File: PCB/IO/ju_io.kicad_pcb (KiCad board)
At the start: 2 copper layers, 30 x 65 mm, 17 parts, among them J1 Conn_01x05, J2 Conn_01x05, J3 Conn_01x05, J4 Conn_01x05, J5 Conn_01x03, J6 Conn_01x03, U1 PiPico_No_SWD

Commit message: PCBs of v1.1
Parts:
- removed J6: Conn_01x03, ju_io:SH1.0_3P
- added D1: WS2812B_Unified, ju_io:WS2812B-2835, F.Cu at (138.6, 121.7)
- added D2: WS2812B_Unified, ju_io:WS2812B-2835, F.Cu at (138.6, 110.7)
- added D3: WS2812B_Unified, ju_io:WS2812B-2835, F.Cu at (138.6, 99.7)
- added D4: WS2812B_Unified, ju_io:WS2812B-2835, F.Cu at (138.6, 88.7)
- U1: footprint ju_io:RPi_Pico_SMD_Pins_No_SWD -> ju_io:RPi_Pico_SMD_Pins_No_SWD_No_Text
- moved R3 34.0 mm to (130.5, 128.6), turned to 0 degrees
- moved R4 28.8 mm to (143.2, 76.8), turned to 0 degrees
- moved J5 25.1 mm to (146.1, 70.7), turned to 180 degrees
- moved J1 12.4 mm to (145.1, 85.7)
- moved J2 12.4 mm to (145.1, 96.7)
- moved R2 5.91 mm to (128.9, 77.8), turned to 180 degrees
- moved R1 5.75 mm to (128.9, 76.2), turned to 180 degrees
- moved C1 4.76 mm to (141.7, 105.4), turned to 0 degrees
- moved J3 4.24 mm to (145.1, 112.7)
- moved J4 4.24 mm to (145.1, 123.7)
- moved B1 3.50 mm to (130.6, 88.7)
- moved B2 3.50 mm to (130.6, 99.7)
- moved B3 3.50 mm to (130.6, 110.7)
- moved B4 3.50 mm to (130.6, 121.7)
- moved U1 3.00 mm to (137.1, 105.7)
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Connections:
- R3 pad 2: Net-(J5-Pin_2) -> Net-(D1-In)
- R4 pad 1: Net-(U1-GPIO16) -> Net-(U1-GPIO28_ADC2)
- R4 pad 2: Net-(J6-Pin_2) -> Net-(J5-Pin_2)
- U1 pad 21: Net-(U1-GPIO16) -> unconnected-(U1-GPIO16-Pad21)
- U1 pad 34: unconnected-(U1-GPIO28_ADC2-Pad34) -> Net-(U1-GPIO28_ADC2)
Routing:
- net Net-(U1-GPIO17): track 40.0 -> 2.83 mm
- net Net-(U1-GPIO16): track 32.4 -> 0.00 mm, vias 1 -> 0
- net Net-(U1-GPIO28_ADC2): track 0.00 -> 28.0 mm, vias 0 -> 1
- net +5V: track 40.5 -> 68.4 mm, vias 2 -> 1
- net Net-(J2-Pin_1): track 29.0 -> 8.01 mm
- net Net-(J2-Pin_3): track 20.5 -> 3.85 mm
- net GND: track 33.0 -> 16.4 mm, vias 15 -> 17
- net Net-(J1-Pin_1): track 27.5 -> 12.0 mm
- net Net-(J2-Pin_2): track 26.1 -> 11.1 mm
- net Net-(J1-Pin_2): track 24.3 -> 10.2 mm
- net Net-(J1-Pin_3): track 18.5 -> 4.46 mm
- net Net-(D1-In): track 0.00 -> 11.2 mm
- net Net-(B4-A): track 0.00 -> 10.3 mm
- net Net-(J2-Pin_4): track 18.5 -> 9.79 mm
- net Net-(D3-Out): track 0.00 -> 8.55 mm
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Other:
- board size 30 x 65 mm -> 26 x 65 mm
- board text added: "IO v1.1"
- board text removed: "IO v1.0"
- board text removed: "JLCJLCJLCJLC"

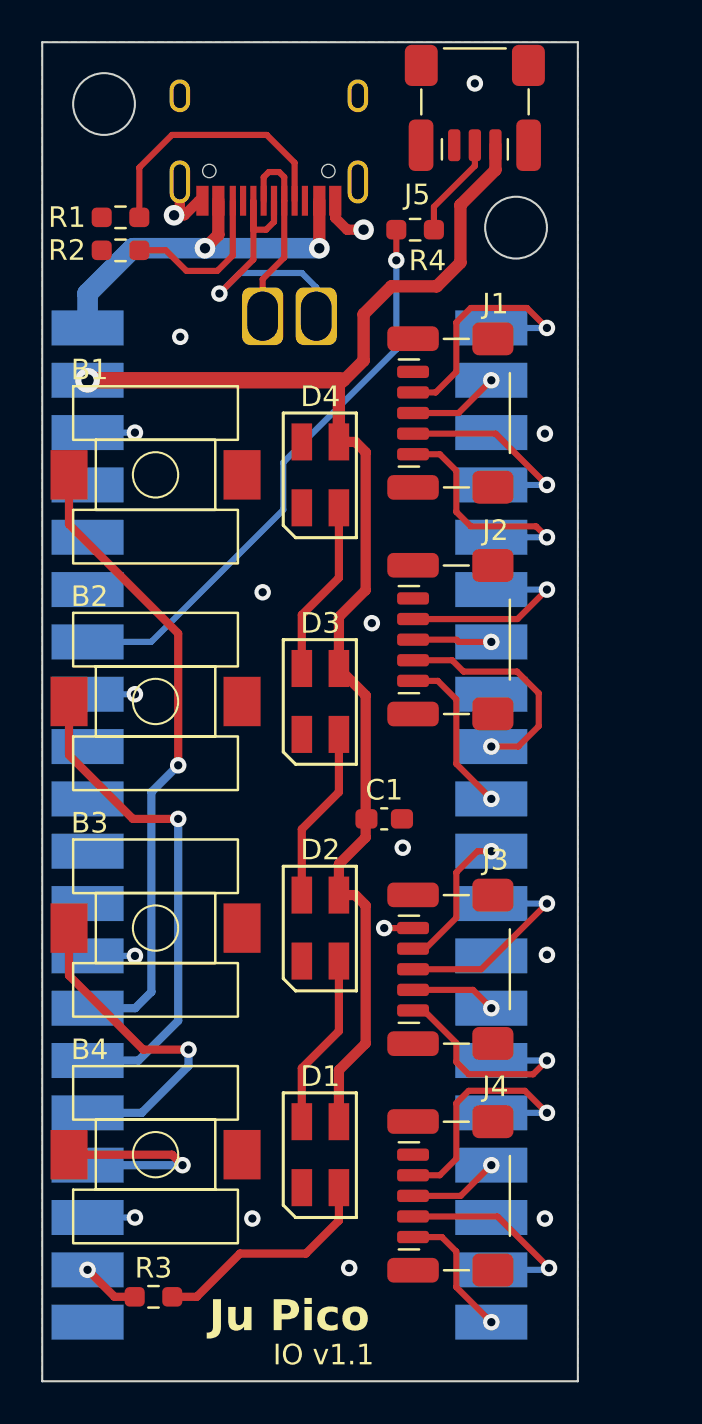
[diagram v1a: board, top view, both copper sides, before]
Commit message: PCB optimization button v1.2, io v1.21
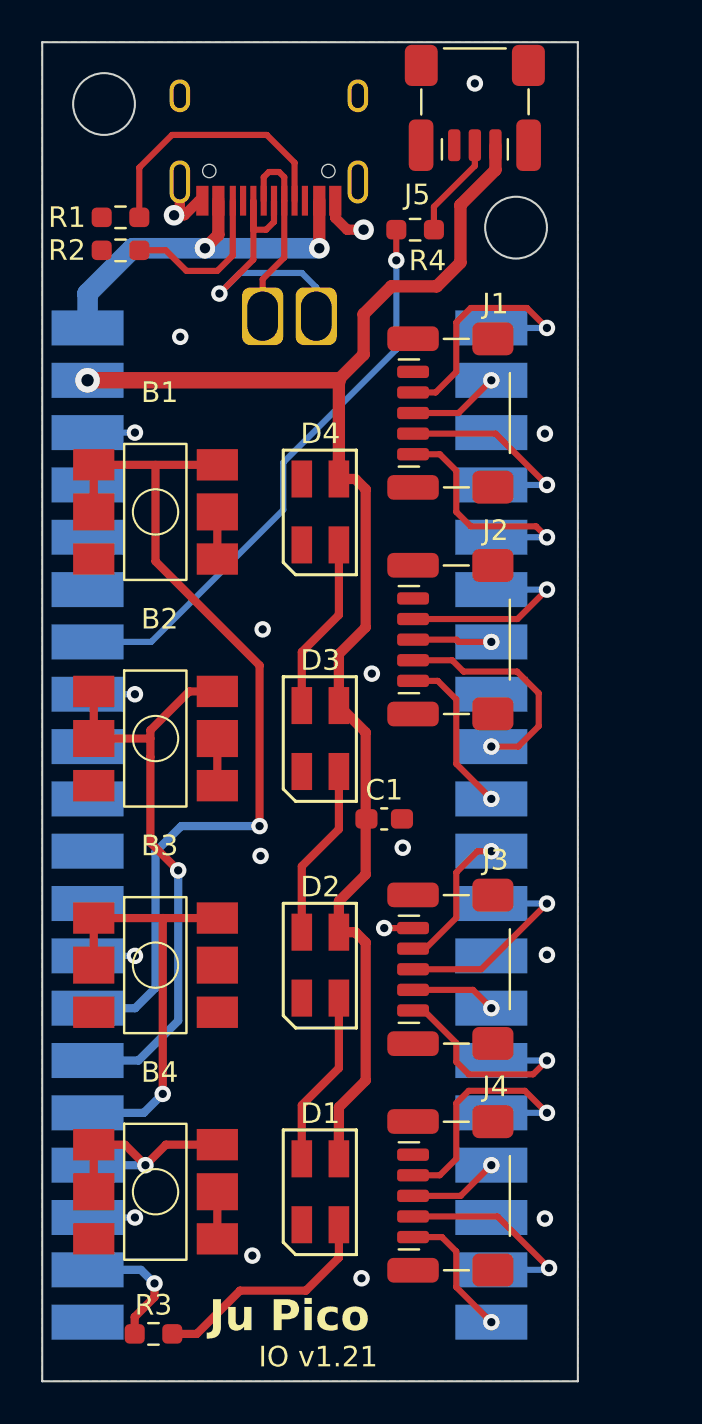
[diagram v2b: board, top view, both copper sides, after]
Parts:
- B1, B2, B3, B4: footprint ju_io:SKSTAAE010 -> ju_io:EVQP1K05M
- moved B1 1.80 mm to (130.6, 90.5)
- moved B2 1.80 mm to (130.6, 101.5)
- moved B3 1.80 mm to (130.6, 112.5)
- moved B4 1.80 mm to (130.6, 123.5)
- moved D1 1.80 mm to (138.6, 123.5)
- moved D2 1.80 mm to (138.6, 112.5)
- moved D3 1.80 mm to (138.6, 101.5)
- moved D4 1.80 mm to (138.6, 90.5)
- moved R3 1.80 mm to (130.5, 130.4)
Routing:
- net Net-(B1-A): track 31.3 -> 43.8 mm
- net GND: track 16.4 -> 23.3 mm, vias 17 -> 18
- net Net-(B2-A): track 24.2 -> 28.9 mm
- net Net-(B3-A): track 16.2 -> 20.9 mm
- net Net-(U1-GPIO17): track 2.83 -> 6.37 mm
- net +5V: track 68.4 -> 70.0 mm
- net Net-(B4-A): track 10.3 -> 11.9 mm
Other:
- board text added: "IO v1.21"
- board text removed: "IO v1.1"

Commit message: Ju Pico IO PCB v1.22
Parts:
- removed R3, R4: 10, Resistor_SMD:R_0603_1608Metric_Pad0.98x0.95mm_HandSolder
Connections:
- U1 pad 22: Net-(U1-GPIO17) -> Net-(D1-In)
- U1 pad 34: Net-(U1-GPIO28_ADC2) -> Net-(J5-Pin_2)
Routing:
- net Net-(J5-Pin_2): track 4.92 -> 33.7 mm, vias 0 -> 1
- net Net-(U1-GPIO28_ADC2): track 28.0 -> 0.00 mm, vias 1 -> 0
- net Net-(U1-GPIO17): track 6.37 -> 0.00 mm, vias 1 -> 0
- net Net-(D1-In): track 11.2 -> 14.6 mm, vias 0 -> 1
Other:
- board text added: "IO v1.22"
- board text removed: "IO v1.21"

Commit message: Ju IO PCB v1.3 (just text change)
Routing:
- net +5V: track 70.0 -> 69.4 mm
- net Net-(J5-Pin_2): track 33.7 -> 34.2 mm
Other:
- board text added: "Ju Pico IO v1.3"
- board text added: "github.com/whowechina"
- board text removed: "IO v1.22"
- board text removed: "Ju Pico"
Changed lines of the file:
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@@
 			(psa4output no)
 			(plot_black_and_white yes)
-			(plotinvisibletext no)
 			(sketchpadsonfab no)
 			(plotpadnumbers no)
@@
 			(at 0 3.98 0)
 			(layer "F.Fab")
+			(hide yes)
 			(effects
 				(font
@@
 			(layer "B.Fab")
 		)
-		(fp_text user "Copper Keepouts shown on Dwgs layer"
-			(at 0.1 30.2 0)
-			(layer "Cmts.User")
-			(hide yes)
-			(effects
-				(font
-					(size 1 1)
-					(thickness 0.15)
-				)
-			)
-		)
 		(fp_text user "${REFERENCE}"
 			(at 0 0 0)
@@
 		(layer "Edge.Cuts")
 	)
-	(gr_text "IO v1.22"
-		(at 135.32 132.08 0)
+	(gr_text "github.com/whowechina"
+		(at 128.35 131.66 0)
 		(layer "F.SilkS")
 		(effects
@@
 		)
 	)
-	(gr_text "Ju Pico"
-		(at 133.17 130.38 0)
+	(gr_text "Ju Pico IO v1.3"
+		(at 129.95 130.18 0)
 		(layer "F.SilkS")
 		(effects
 			(font
-				(size 1.5 1.5)
-				(thickness 0.3)
+				(size 1.25 1.25)
+				(thickness 0.24)
 				(bold yes)
 			)
@@
 	)
 	(segment
+		(start 145.37 75.85)
+		(end 147.07 74.15)
+		(width 0.6)
+		(layer "F.Cu")
+		(net 2)
+	)
+	(segment
 		(start 139.47 99.88)
 		(end 140.77 101.18)
@@
 	)
 	(segment
-		(start 145.37 75.58)
-		(end 147.07 73.88)
+		(start 140.67 82.84)
+		(end 140.67 80.88)
 		(width 0.6)
 		(layer "F.Cu")
@@
 	)
 	(segment
-		(start 139.47 84.14)
-		(end 139.47 88.88)
+		(start 140.67 80.88)
+		(end 142.02 79.53)
 		(width 0.6)
 		(layer "F.Cu")
@@
 	)
 	(segment
-		(start 140.27 110.88)
-		(end 140.77 111.38)
-		(width 0.5)
+		(start 143.14 79.53)
+		(end 145.37 77.3)
+		(width 0.6)
 		(layer "F.Cu")
 		(net 2)
 	)
 	(segment
-		(start 139.42 84.09)
-		(end 140.67 82.84)
+		(start 147.07 74.15)
+		(end 147.07 72.68)
 		(width 0.6)
 		(layer "F.Cu")
@@
 	)
 	(segment
-		(start 140.67 80.88)
-		(end 142.02 79.53)
+		(start 139.47 84.14)
+		(end 139.47 88.88)
 		(width 0.6)
 		(layer "F.Cu")
@@
 	)
 	(segment
-		(start 140.77 108.08)
-		(end 139.47 109.38)
+		(start 140.27 110.88)
+		(end 140.77 111.38)
 		(width 0.5)
 		(layer "F.Cu")
@@
 	)
 	(segment
-		(start 145.37 78.38)
-		(end 145.37 75.58)
-		(width 0.6)
-		(layer "F.Cu")
-		(net 2)
-	)
-	(segment
-		(start 147.07 73.88)
-		(end 147.07 72.68)
-		(width 0.6)
+		(start 140.77 108.08)
+		(end 139.47 109.38)
+		(width 0.5)
 		(layer "F.Cu")
 		(net 2)
@@
 	)
 	(segment
+		(start 142.02 79.53)
+		(end 143.14 79.53)
+		(width 0.6)
+		(layer "F.Cu")
+		(net 2)
+	)
+	(segment
 		(start 139.47 119.38)
 		(end 139.47 121.88)
@@
 	)
 	(segment
-		(start 144.22 79.53)
-		(end 145.37 78.38)
-		(width 0.6)
-		(layer "F.Cu")
-		(net 2)
-	)
-	(segment
-		(start 140.67 82.84)
-		(end 140.67 80.88)
+		(start 145.37 77.3)
+		(end 145.37 75.85)
 		(width 0.6)
 		(layer "F.Cu")
@@
 	)
 	(segment
-		(start 142.02 79.53)
-		(end 144.22 79.53)
+		(start 139.42 84.09)
+		(end 140.67 82.84)
 		(width 0.6)
 		(layer "F.Cu")
@@
 	)
 	(segment
-		(start 142.2575 78.2675)
-		(end 142.2575 77.4925)
+		(start 146.07 73.93)
+		(end 144.53 75.47)
+		(width 0.3)
+		(layer "F.Cu")
+		(net 34)
+	)
+	(segment
+		(start 144.53 76.89)
+		(end 143.1525 78.2675)
+		(width 0.3)
+		(layer "F.Cu")
+		(net 34)
+	)
+	(segment
+		(start 146.07 72.68)
+		(end 146.07 73.93)
 		(width 0.3)
 		(layer "F.Cu")
@@
 	)
 	(segment
-		(start 142.2575 77.4925)
-		(end 146.07 73.68)
+		(start 143.1525 78.2675)
+		(end 142.2575 78.2675)
 		(width 0.3)
 		(layer "F.Cu")
@@
 	)
 	(segment
-		(start 146.07 73.68)
-		(end 146.07 72.68)
+		(start 144.53 75.47)
+		(end 144.53 76.89)
 		(width 0.3)
 		(layer "F.Cu")
@@
 		(layer "F.Cu")
 		(name "$teardrop_padvia$")
-		(hatch full 0.1)
+		(hatch none 0.1)
 		(priority 30000)
 		(attr
@@
 		(layer "B.Cu")
 		(name "$teardrop_padvia$")
-		(hatch full 0.1)
+		(hatch none 0.1)
 		(priority 30000)
 		(attr
